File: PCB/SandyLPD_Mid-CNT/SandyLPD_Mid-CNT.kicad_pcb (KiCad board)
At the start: 2 copper layers, 113.1 x 58.7 mm, 55 parts

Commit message: Base→MId中央のネジ位置を1箇所変更
Mid中央をリバーシブルにすると、ソケットのパッドと干渉が出たため。
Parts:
- removed EXT_MC2, EXT_MC3: Conn_01x01, locallib:TestPoint_THTPad_D2.0mm_Drill1.0mm
- removed the REF** at (125.8, 52.7)
- removed the REF** at (201.9, 52.7)
- removed the REF** at (166.3, 71.1)
- removed the REF** at (194.8, 62.3)
- removed the REF** at (180.5, 81.4)
- removed the REF** at (133.4, 56.6)
- removed the REF** at (194.8, 57.0)
- removed the REF** at (201.9, 46.3)
- removed the REF** at (170.4, 86.9)
- removed the REF** at (180.5, 76.1)
- removed the REF** at (125.8, 46.3)
- removed the REF** at (183.0, 62.7)
- removed the REF** at (164.0, 75.5)
- removed the REF** at (144.9, 50.8)
- removed the REF** at (132.9, 62.3)
- removed the REF** at (168.4, 92.4)
- removed the REF** at (183.0, 50.8)
- added REF**: ICON_Screw_Medium, locallib:ICON_Screw_Medium, B.Cu at (155.1, 91.5)
- Cutout1: footprint locallib:SandyLP_outline_Mid -> locallib:SandyLPD_outline_Mid-CNT
- H1, H_top_2: moved to F.Cu
- SW_H1, SW_U1: footprint locallib:Kailh_socket_ChocV2_small_#2pad -> locallib:Kailh_socket_ChocV2; moved to B.Cu
- SW_MACRO_L1: footprint locallib:Kailh_socket_ChocV2_narrow_#2pad -> locallib:Kailh_socket_ChocV2_small_#2pad
- SW_MACRO_R1: footprint locallib:Kailh_socket_ChocV2_narrow_#2pad -> locallib:Kailh_socket_ChocV2; moved to B.Cu
- T_C4: renamed from EXT_MC1; moved to B.Cu
- T_C5: renamed from EXT_MC5; moved to B.Cu
- moved T_C4 121.8 mm to (112.1, 76.5), turned to 180 degrees
- moved T_C5 121.8 mm to (112.1, 80.6), turned to 180 degrees
- moved SW_MACRO_R1 109.2 mm to (144.9, 87.7), turned to 180 degrees
- moved D1 98.9 mm to (121.1, 48.4), turned to -90 degrees
- moved SW_U1 91.2 mm to (116.3, 49.6), turned to 180 degrees
- moved SW_H1 90.1 mm to (135.4, 68.7), turned to 180 degrees
- moved D4 88.3 mm to (149.6, 86.5), turned to -90 degrees
- moved D2 87.1 mm to (140.1, 67.5), turned to -90 degrees
- moved REF** 81.8 mm to (122.3, 15.2)
- moved REF** 81.8 mm to (118.9, 4.18)
- moved REF** 81.8 mm to (119.1, -2.29)
- moved REF** 81.8 mm to (117.5, -14.9)
- moved REF** 81.8 mm to (117.8, -14.9)
- moved REF** 81.8 mm to (124.3, 9.72)
- moved H1 61.8 mm to (109.8, 38.9), turned to 0 degrees
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- renumbered EXT_MR0 to T_R0, EXT_MR5 to T_R1, EXT_MR2 to T_R2
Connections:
- SW_G1 pad 1: Mid_col4 -> Mid_col5
- SW_H1 pad 1: Mid_col4 -> Mid_col5
- SW_MACRO_L1 pad 1: Mid_col4 -> Mid_col5
- SW_MACRO_R1 pad 1: Mid_col4 -> Mid_col5
- SW_R1 pad 1: Mid_col3 -> Mid_col4
- SW_U1 pad 1: Mid_col3 -> Mid_col4
- T_C4 pad 1: Mid_col3 -> Mid_col4
- T_C5 pad 1: Mid_col4 -> Mid_col5
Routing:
- net Mid_col2: track 139.5 -> 0.00 mm
- net Mid_col4: track 133.2 -> 0.00 mm, vias 3 -> 0
- net Mid_row1: track 124.6 -> 0.00 mm, vias 1 -> 0
- net (no net): track 67.5 -> 0.00 mm
- net Mid_row0: track 37.6 -> 0.00 mm
- net Mid_row2: track 31.0 -> 0.00 mm
- net Net-(D12-A): track 4.88 -> 0.00 mm
- net Net-(D4-A): track 4.88 -> 0.00 mm
- net Net-(D7-A): track 4.62 -> 0.00 mm
- net Net-(D3-A): track 4.59 -> 0.00 mm
- net Mid_col3: vias 2 -> 0
- net GND: vias 30 -> 0
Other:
- board size 113.1 x 58.7 mm -> 49.4 x 61 mm

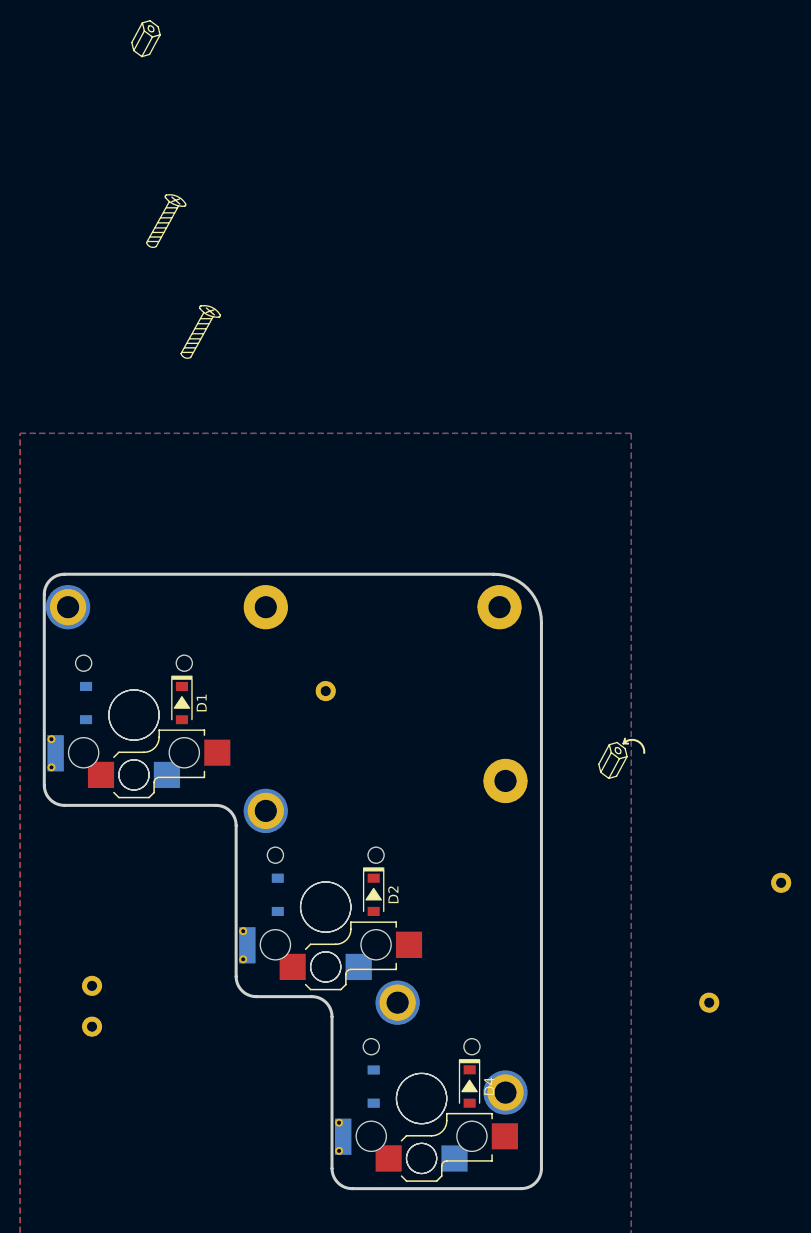
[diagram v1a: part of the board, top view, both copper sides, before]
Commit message: Mid中央、配線やシルク調整中。
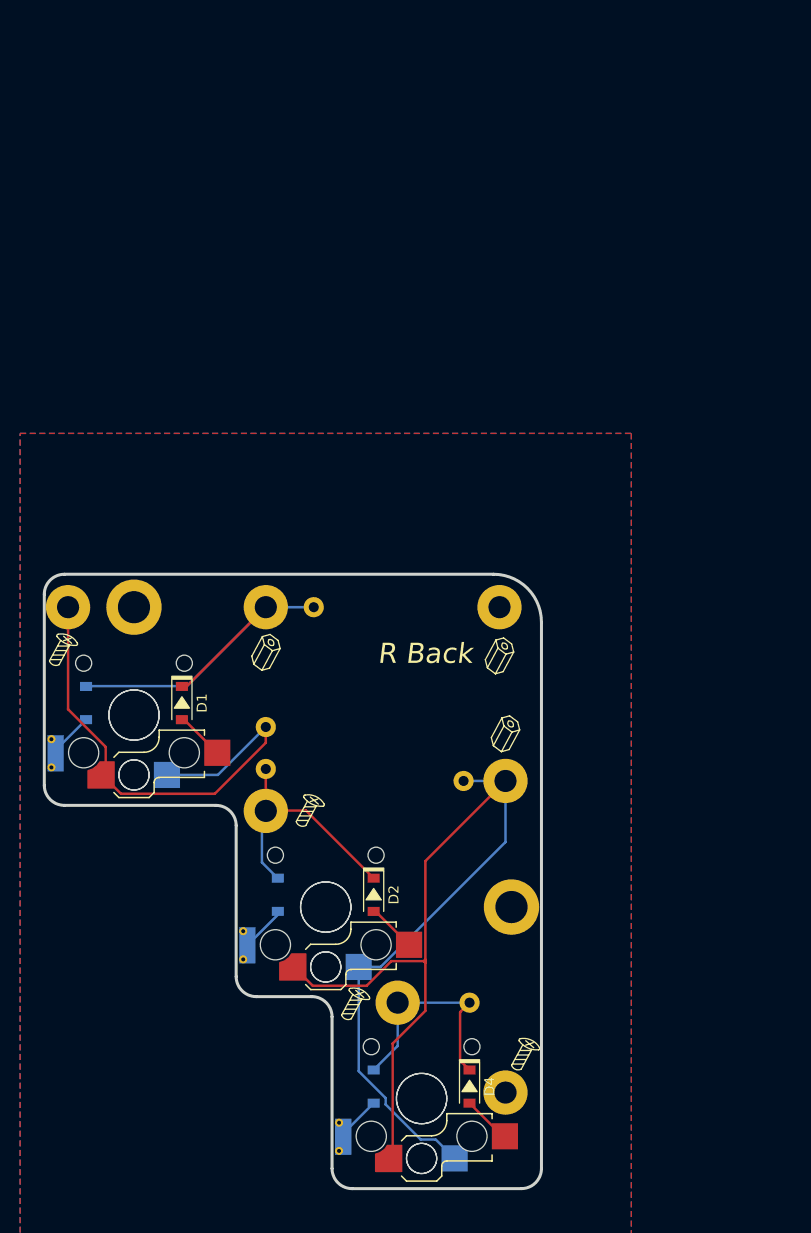
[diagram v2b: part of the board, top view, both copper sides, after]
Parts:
- removed the REF** at (117.5, -14.9)
- removed the REF** at (122.3, 15.2)
- removed the REF** at (166.3, 52.3)
- removed the REF** at (118.9, 4.18)
- removed the REF** at (117.8, -14.9)
- removed the REF** at (119.1, -2.29)
- removed the REF** at (124.3, 9.72)
- added H5: MountingHole, locallib:MountingHole_M2_Through-hole_tap_THC-0.8-x-2, F.Cu at (116.3, 38.9)
- added H6: MountingHole, locallib:MountingHole_M2_Through-hole_tap_THC-0.8-x-2, F.Cu at (153.8, 68.7)
- added REF**: ICON_Screw_Medium, locallib:ICON_Screw_Medium, F.Cu at (109.2, 45.7)
- added REF**: ICON_Spacer, locallib:ICON_Spacer, B.Cu at (153.2, 54.1)
- added REF**: ICON_Spacer, locallib:ICON_Spacer, B.Cu at (129.4, 46.0)
- added REF**: ICON_Spacer, locallib:ICON_Spacer, F.Cu at (152.7, 46.4)
- added REF**: ICON_Spacer, locallib:ICON_Spacer, F.Cu at (153.3, 54.1)
- added REF**: ICON_Screw_Medium, locallib:ICON_Screw_Medium, F.Cu at (133.7, 61.7)
- added REF**: ICON_Screw_Medium, locallib:ICON_Screw_Medium, F.Cu at (138.2, 80.9)
- added REF**: ICON_Screw_Medium, locallib:ICON_Screw_Medium, F.Cu at (155.1, 85.9)
- added REF**: ICON_Spacer, locallib:ICON_Spacer, B.Cu at (152.6, 46.4)
- H1, H2, H3, H4: footprint locallib:MountingHole_1.8-2.2mm_M2_Pad_minimal -> locallib:MountingHole_2.2mm_M2_Pad_minimal
- SW_H1, SW_MACRO_R1, SW_U1: footprint locallib:Kailh_socket_ChocV2 -> locallib:Kailh_socket_ChocV2_for_Reverse
- moved T_R1 52.4 mm to (129.4, 55.0), turned to 180 degrees
- moved T_C5 44.2 mm to (149.1, 56.2)
- moved REF** 36.1 mm to (129.5, 46.0)
- moved T_C4 31.0 mm to (129.4, 50.8)
- moved T_R2 23.8 mm to (149.6, 78.2)
- moved REF** 8.49 mm to (138.3, 80.8)
- moved T_R0 8.42 mm to (134.2, 38.9)
- moved REF** 6.47 mm to (109.1, 45.7)
- moved REF** 5.61 mm to (154.7, 85.9)
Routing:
- net Mid_col5: track 0.00 -> 111.0 mm
- net Mid_col4: track 0.00 -> 50.6 mm
- net Mid_row0: track 0.00 -> 37.5 mm
- net Mid_row1: track 0.00 -> 25.2 mm
- net Mid_row2: track 0.00 -> 22.3 mm
- net Net-(D2-A): track 0.00 -> 4.89 mm
- net Net-(D1-A): track 0.00 -> 4.88 mm
- net Net-(D4-A): track 0.00 -> 4.88 mm
- net Net-(D7-A): track 0.00 -> 4.62 mm
- net Net-(D3-A): track 0.00 -> 4.59 mm
- net Net-(D12-A): track 0.00 -> 4.59 mm
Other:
- board text added: "#SandyLP_Duo DN0010 Mid-CNT"
- board text added: "L Back"
- board text added: "R Back"
- board text removed: "#SandyLP_kbd DN0010 Mid by @jpskenn"
- board text removed: "Back Side"

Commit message: パーツ配置完了。ネジ位置調整中。
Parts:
- SW_G1, SW_MACRO_L1, SW_R1: footprint locallib:Kailh_socket_ChocV2_small_#2pad -> locallib:Kailh_socket_ChocV2_small_#2pad_for_Reverse_no_hole
- moved D1 9.53 mm to (121.1, 48.4)
- moved D3 9.53 mm to (140.1, 67.5)
- moved D5 9.10 mm to (149.2, 86.5)
- moved REF** 8.93 mm to (153.2, 63.0)
- moved REF** 8.93 mm to (153.3, 63.0)
- moved REF** 7.91 mm to (146.2, 80.2)
- moved REF** 7.74 mm to (146.0, 80.9)
- moved REF** 0.84 mm to (132.9, 61.7)
- moved REF** 0.84 mm to (133.1, 61.1)
- moved REF** 0.60 mm to (152.7, 45.8)
- moved REF** 0.60 mm to (152.6, 45.8)
- moved D6 0.43 mm to (149.2, 86.5)
- moved REF** 0.42 mm to (154.9, 85.5)
- moved REF** 0.32 mm to (154.5, 86.1)
- moved REF** 0.25 mm to (129.4, 45.8)
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- renumbered D3 to D1, D1 to D2, D7 to D3, D2 to D4, D12 to D5, D4 to D6, T_R0 to T_R1, T_R1 to T_R2, T_R2 to T_R3
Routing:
- net Net-(D5-A): track 4.59 -> 23.3 mm
- net Net-(D1-A): track 4.59 -> 15.3 mm
- net Net-(D3-A): track 4.62 -> 14.9 mm
- net Mid_row0: track 37.5 -> 28.0 mm
- net Mid_row1: track 25.2 -> 31.2 mm
- net Mid_col5: track 111.0 -> 113.6 mm
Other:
- board text added: "#SandyLP_Duo DN0010"
- board text removed: "#SandyLP_Duo DN0010 Mid-CNT"

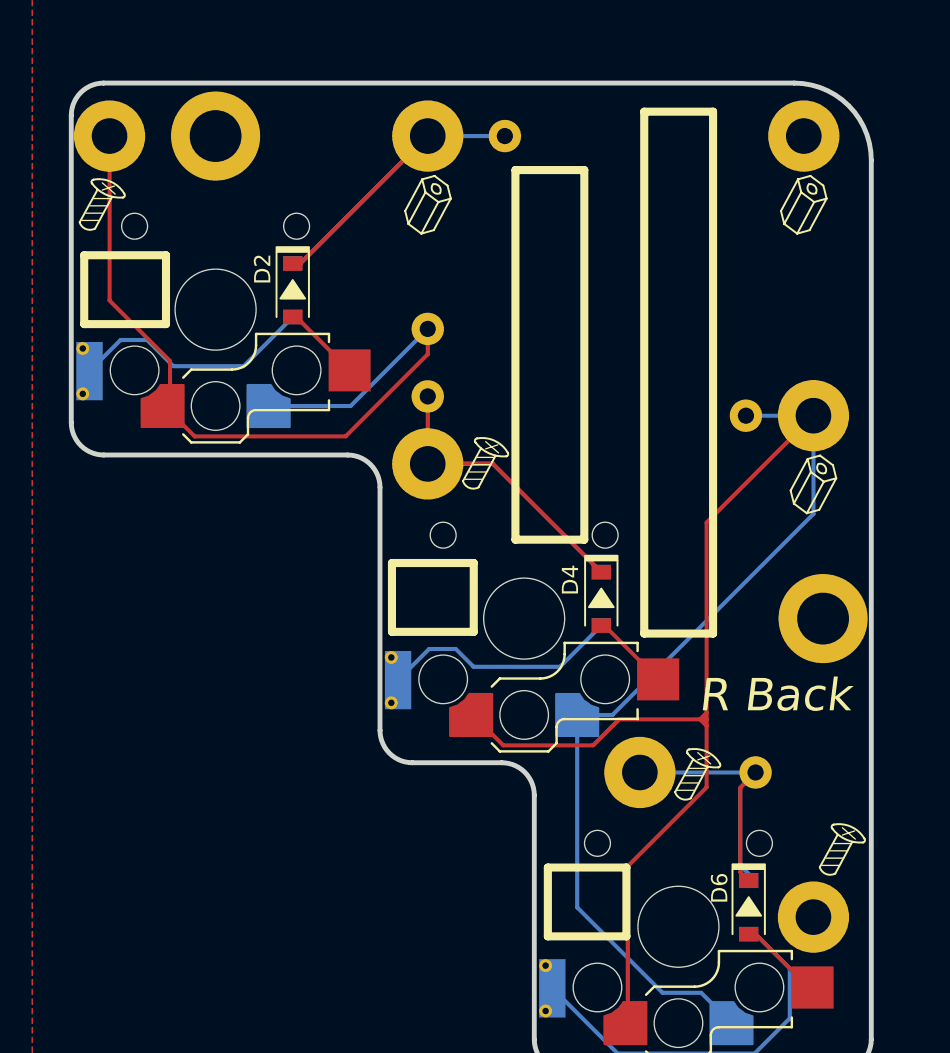
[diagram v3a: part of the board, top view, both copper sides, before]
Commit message: スルーホールタップの接続先を変更・調整 #19
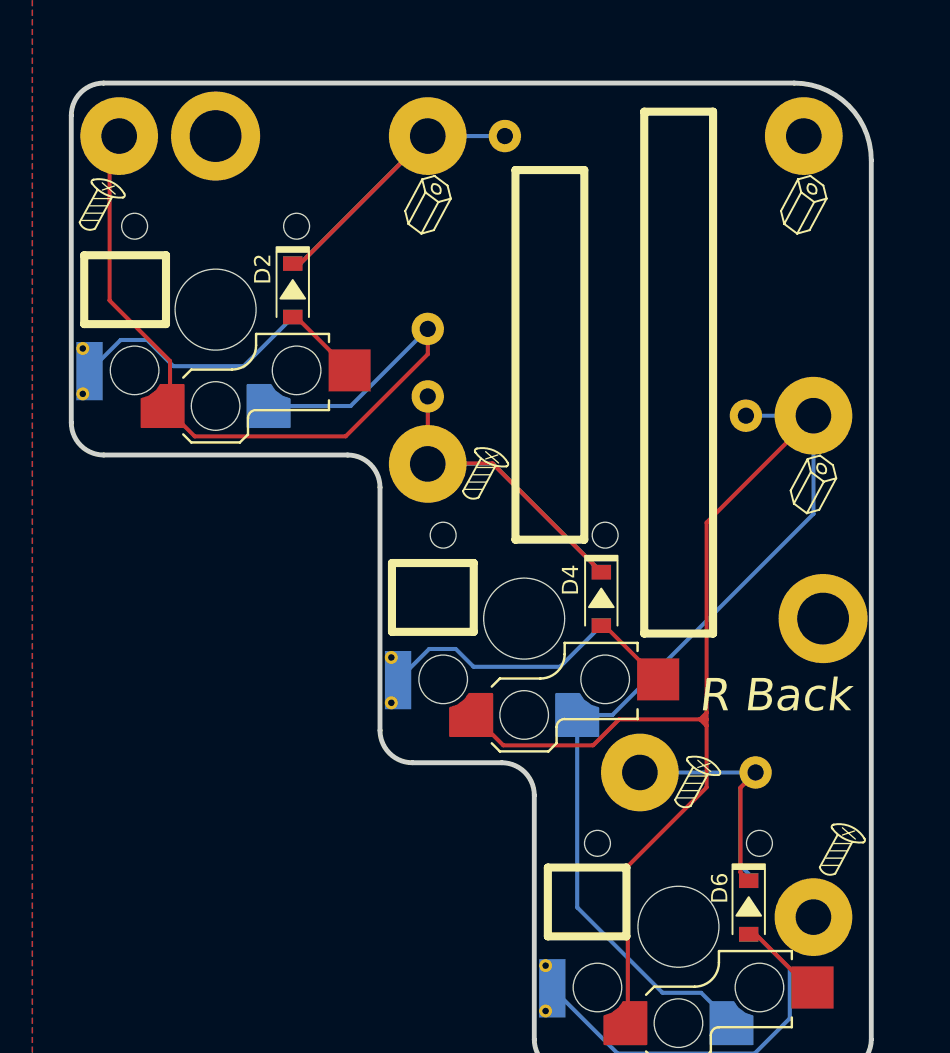
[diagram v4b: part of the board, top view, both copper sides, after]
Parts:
- H1, H2, H3, H4, H_top_1, H_top_2, H_top_3: footprint locallib:MountingHole_2.2mm_M2_Pad_minimal -> locallib:MountingHole_2.2-4.8mm_M2_Pad_minimal_for_Through-hole_tap
- moved REF** 0.62 mm to (132.9, 62.3)
- moved REF** 0.60 mm to (146.2, 79.6)
- moved REF** 0.60 mm to (133.1, 60.5)
- moved H1 0.60 mm to (110.4, 38.9)
- moved REF** 0.47 mm to (146.0, 81.4)
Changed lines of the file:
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@@
 	(net 11 "Mid_row0")
 	(net 12 "GND")
-	(footprint "locallib:MountingHole_2.2mm_M2_Pad_minimal"
+	(footprint "locallib:MountingHole_2.2-4.8mm_M2_Pad_minimal_for_Through-hole_tap"
 		(layer "F.Cu")
 		(at 153.217917 87.130009)
@@
 			)
 		)
-		(property "Footprint" "locallib:MountingHole_2.2mm_M2_Pad_minimal"
+		(property "Footprint" "locallib:MountingHole_2.2-4.8mm_M2_Pad_minimal_for_Through-hole_tap"
 			(at 0 0 0)
 			(layer "F.Fab")
@@
 		(fp_circle
 			(center 0 0)
-			(end 2.2 0)
+			(end 2.4 0)
 			(stroke
 				(width 0.15)
@@
 		(pad "1" thru_hole circle
 			(at 0 0)
-			(size 4.4 4.4)
+			(size 4.8 4.8)
 			(drill 2.2)
 			(layers "*.Cu" "*.Mask")
@@
 		)
 	)
-	(footprint "locallib:MountingHole_2.2mm_M2_Pad_minimal"
+	(footprint "locallib:MountingHole_2.2-4.8mm_M2_Pad_minimal_for_Through-hole_tap"
 		(layer "F.Cu")
 		(at 129.40531 59.15028)
@@
 			)
 		)
-		(property "Footprint" "locallib:MountingHole_2.2mm_M2_Pad_minimal"
+		(property "Footprint" "locallib:MountingHole_2.2-4.8mm_M2_Pad_minimal_for_Through-hole_tap"
 			(at 0 0 0)
 			(layer "F.Fab")
@@
 		(fp_circle
 			(center 0 0)
-			(end 2.2 0)
+			(end 2.4 0)
 			(stroke
 				(width 0.15)
@@
 		(pad "1" thru_hole circle
 			(at 0 0)
-			(size 4.4 4.4)
+			(size 4.8 4.8)
 			(drill 2.2)
 			(layers "*.Cu" "*.Mask")
@@
 		)
 	)
-	(footprint "locallib:MountingHole_2.2mm_M2_Pad_minimal"
+	(footprint "locallib:MountingHole_2.2-4.8mm_M2_Pad_minimal_for_Through-hole_tap"
 		(layer "F.Cu")
-		(at 109.760068 38.909656)
+		(at 110.355381 38.909656)
 		(descr "Mounting Hole 2.2mm, M2")
 		(tags "mounting hole 2.2mm m2")
@@
 			)
 		)
-		(property "Footprint" "locallib:MountingHole_2.2mm_M2_Pad_minimal"
+		(property "Footprint" "locallib:MountingHole_2.2-4.8mm_M2_Pad_minimal_for_Through-hole_tap"
 			(at 0 0 0)
 			(layer "F.Fab")
@@
 		(fp_circle
 			(center 0 0)
-			(end 2.2 0)
+			(end 2.4 0)
 			(stroke
 				(width 0.15)
@@
 		(pad "1" thru_hole circle
 			(at 0 0)
-			(size 4.4 4.4)
+			(size 4.8 4.8)
 			(drill 2.2)
 			(layers "*.Cu" "*.Mask")
@@
 		)
 	)
-	(footprint "locallib:MountingHole_2.2mm_M2_Pad_minimal"
+	(footprint "locallib:MountingHole_2.2-4.8mm_M2_Pad_minimal_for_Through-hole_tap"
 		(layer "F.Cu")
 		(at 142.502283 78.200314)
@@
 			)
 		)
-		(property "Footprint" "locallib:MountingHole_2.2mm_M2_Pad_minimal"
+		(property "Footprint" "locallib:MountingHole_2.2-4.8mm_M2_Pad_minimal_for_Through-hole_tap"
 			(at 0 0 0)
 			(layer "F.Fab")
@@
 		(fp_circle
 			(center 0 0)
-			(end 2.2 0)
+			(end 2.4 0)
 			(stroke
 				(width 0.15)
@@
 		(pad "1" thru_hole circle
 			(at 0 0)
-			(size 4.4 4.4)
+			(size 4.8 4.8)
 			(drill 2.2)
 			(layers "*.Cu" "*.Mask")
@@
 		)
 	)
-	(footprint "locallib:MountingHole_2.2mm_M2_Pad_minimal"
+	(footprint "locallib:MountingHole_2.2-4.8mm_M2_Pad_minimal_for_Through-hole_tap"
 		(layer "F.Cu")
 		(at 129.405397 38.909656 180)
@@
 			)
 		)
-		(property "Footprint" "locallib:MountingHole_2.2mm_M2_Pad_minimal"
+		(property "Footprint" "locallib:MountingHole_2.2-4.8mm_M2_Pad_minimal_for_Through-hole_tap"
 			(at 0 0 180)
 			(layer "F.Fab")
@@
 		(fp_circle
 			(center 0 0)
-			(end 2.2 0)
+			(end 2.4 0)
 			(stroke
 				(width 0.15)
@@
 		(pad "1" thru_hole circle
 			(at 0 0 180)
-			(size 4.4 4.4)
+			(size 4.8 4.8)
 			(drill 2.2)
 			(layers "*.Cu" "*.Mask")
@@
 		)
 	)
-	(footprint "locallib:MountingHole_2.2mm_M2_Pad_minimal"
+	(footprint "locallib:MountingHole_2.2-4.8mm_M2_Pad_minimal_for_Through-hole_tap"
 		(layer "F.Cu")
 		(at 153.217917 56.173733)
@@
 			)
 		)
-		(property "Footprint" "locallib:MountingHole_2.2mm_M2_Pad_minimal"
+		(property "Footprint" "locallib:MountingHole_2.2-4.8mm_M2_Pad_minimal_for_Through-hole_tap"
 			(at 0 0 0)
 			(layer "F.Fab")
@@
 		(fp_circle
 			(center 0 0)
-			(end 2.2 0)
+			(end 2.4 0)
 			(stroke
 				(width 0.15)
@@
 		(pad "1" thru_hole circle
 			(at 0 0)
-			(size 4.4 4.4)
+			(size 4.8 4.8)
 			(drill 2.2)
 			(layers "*.Cu" "*.Mask")
@@
 		)
 	)
-	(footprint "locallib:MountingHole_2.2mm_M2_Pad_minimal"
+	(footprint "locallib:MountingHole_2.2-4.8mm_M2_Pad_minimal_for_Through-hole_tap"
 		(layer "F.Cu")
 		(at 152.622604 38.909656)
@@
 			)
 		)
-		(property "Footprint" "locallib:MountingHole_2.2mm_M2_Pad_minimal"
+		(property "Footprint" "locallib:MountingHole_2.2-4.8mm_M2_Pad_minimal_for_Through-hole_tap"
 			(at 0 0 0)
 			(layer "F.Fab")
@@
 		(fp_circle
 			(center 0 0)
-			(end 2.2 0)
+			(end 2.4 0)
 			(stroke
 				(width 0.15)
@@
 		(pad "1" thru_hole circle
 			(at 0 0)
-			(size 4.4 4.4)
+			(size 4.8 4.8)
 			(drill 2.2)
 			(layers "*.Cu" "*.Mask")
@@
 		(locked yes)
 		(layer "F.Cu")
-		(at 132.889966 61.698514)
+		(at 132.889966 62.320408)
 		(property "Reference" "REF**"
 			(at 0 0.5 0)
@@
 		(locked yes)
 		(layer "F.Cu")
-		(at 145.986852 80.898514)
+		(at 145.986852 81.370424)
 		(property "Reference" "REF**"
 			(at 0 0.5 0)
@@
 		(tags "test point THT pad")
 		(property "Reference" "T_C4"
-			(at -3.571878 0 360)
+			(at -3.571878 0 0)
 			(layer "B.SilkS")
 			(effects
@@
 		)
 		(property "Value" "Conn_01x01"
-			(at 0 -2.05 360)
+			(at 0 -2.05 0)
 			(layer "B.Fab")
 			(effects
@@
 		)
 		(fp_text user "${REFERENCE}"
-			(at 0 2 360)
+			(at 0 2 0)
 			(layer "B.Fab")
 			(effects
@@
 		(locked yes)
 		(layer "B.Cu")
-		(at 133.064584 61.129782 180)
+		(at 133.064584 60.534469 180)
 		(property "Reference" "REF**"
 			(at 0 -0.5 0)
@@
 		(tags "test point THT pad")
 		(property "Reference" "T_R2"
-			(at -3.571878 0.735923 360)
+			(at -3.571878 0.735923 0)
 			(layer "B.SilkS")
 			(effects
@@
 		)
 		(property "Value" "Conn_01x01"
-			(at 0 -2.05 360)
+			(at 0 -2.05 0)
 			(layer "B.Fab")
 			(effects
@@
 		)
 		(fp_text user "${REFERENCE}"
-			(at 0 2 360)
+			(at 0 2 0)
 			(layer "B.Fab")
 			(effects
@@
 		(tags "test point THT pad")
 		(property "Reference" "T_R1"
-			(at 0 1.998 360)
+			(at 0 1.998 0)
 			(layer "B.SilkS")
 			(effects
@@
 		)
 		(property "Value" "Conn_01x01"
-			(at 0 -2.05 360)
+			(at 0 -2.05 0)
 			(layer "B.Fab")
 			(effects
@@
 		)
 		(fp_text user "${REFERENCE}"
-			(at 0 2 360)
+			(at 0 2 0)
 			(layer "B.Fab")
 			(effects
@@
 		(locked yes)
 		(layer "B.Cu")
-		(at 146.16147 80.179798 180)
+		(at 146.16147 79.584485 180)
 		(property "Reference" "REF**"
 			(at 0 -0.5 0)
@@
 	)
 	(segment
-		(start 113.495935 55.92528)
-		(end 113.495935 52.79403)
+		(start 113.495935 52.79403)
+		(end 109.760068 49.058163)
 		(width 0.25)
 		(layer "F.Cu")
@@
 	)
 	(segment
-		(start 113.495935 52.79403)
-		(end 109.760068 49.058163)
+		(start 115.020935 57.45028)
+		(end 113.495935 55.92528)
 		(width 0.25)
 		(layer "F.Cu")
@@
 	)
 	(segment
-		(start 115.020935 57.45028)
-		(end 113.495935 55.92528)
+		(start 109.760068 39.504969)
+		(end 110.355381 38.909656)
 		(width 0.25)
 		(layer "F.Cu")
@@
 	)
 	(segment
+		(start 113.495935 55.92528)
+		(end 113.495935 52.79403)
+		(width 0.25)
+		(layer "F.Cu")
+		(net 7)
+	)
+	(segment
 		(start 129.405397 50.815916)
 		(end 129.405397 52.382349)
@@
 	(segment
 		(start 109.760068 49.058163)
-		(end 109.760068 38.909656)
+		(end 109.760068 39.504969)
 		(width 0.25)
 		(layer "F.Cu")
